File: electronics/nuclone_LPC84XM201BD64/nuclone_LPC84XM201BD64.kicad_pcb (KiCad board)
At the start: 2 copper layers, 48.3 x 76.2 mm, 53 parts, among them J1 JTAG_2X05, J2 USB-ID, J3 nuclone_small_left, J4 nuclone_small_right, SW1 RESET, U1 MCP1702-MB, U2 LPC845M301JBD48, Y1 12MHz

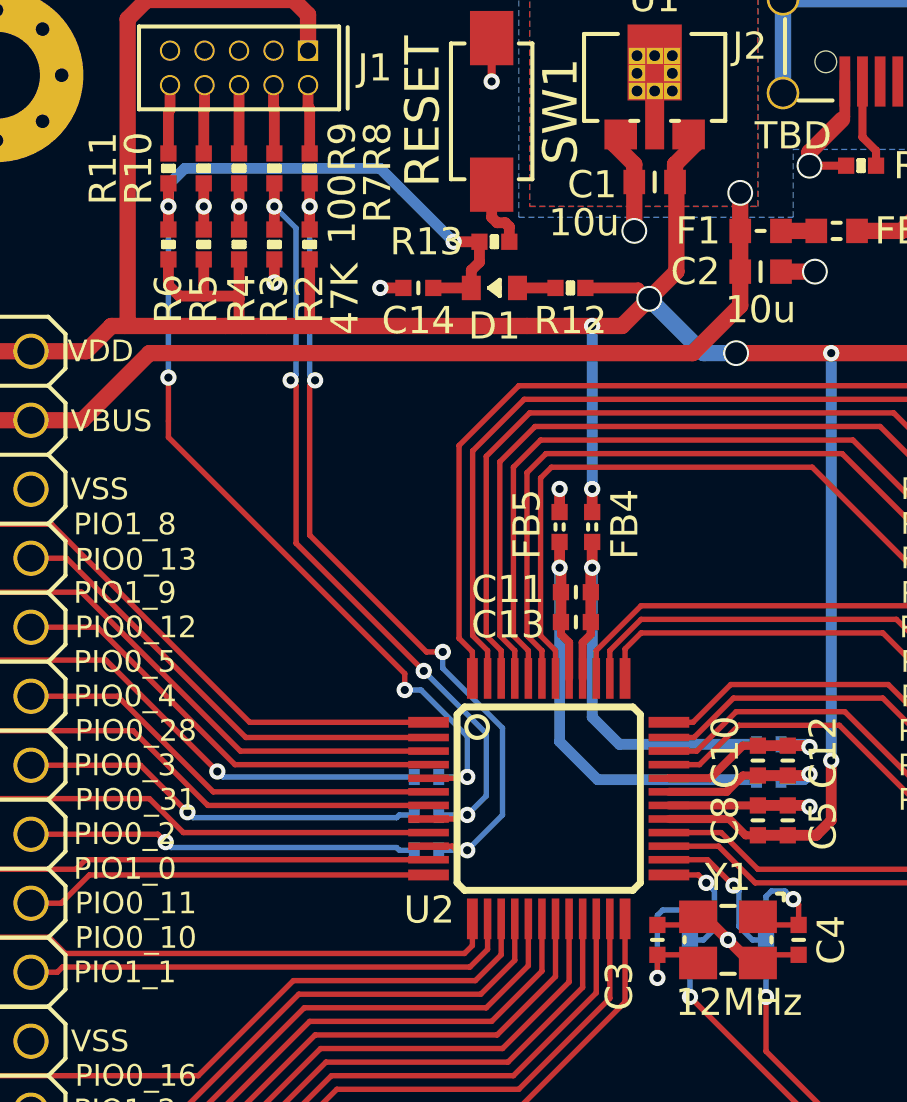
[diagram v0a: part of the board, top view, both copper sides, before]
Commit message: added power led and initial placement, removed old microcontroller
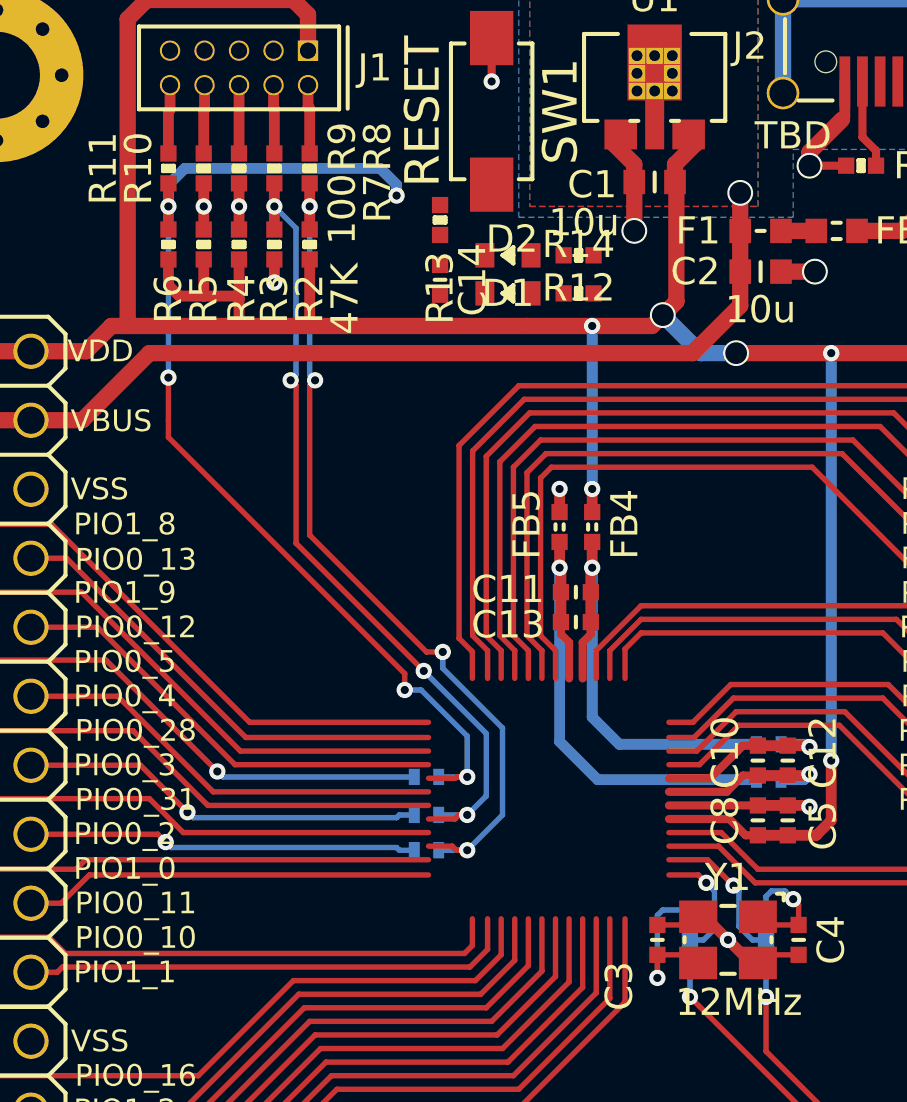
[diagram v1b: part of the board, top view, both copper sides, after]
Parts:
- removed U2: LPC845M301JBD48, SquantorIC:SOT313-2-NXP
- added D2: GREEN, SquantorDiodes:LED_0603_hand, F.Cu at (83.6, 72.8)
- added R14: 10K, SquantorRcl:R_0402_hand, F.Cu at (86.2, 72.8)
- JP1: value PIO0_0 -> PIO0_5
- JP2: value PIO0_10 -> PIO0_3
- JP3: value PIO1_3 -> PIO0_2
- moved R13 2.15 mm to (81.1, 70.1), turned to 90 degrees
- moved D1 1.30 mm to (83.6, 71.4)
- moved R12 1.24 mm to (86.2, 71.4)
- moved C14 0.85 mm to (81.1, 72.3), turned to 90 degrees
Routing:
- net /RESET: track 46.9 -> 40.2 mm
- net /VDD: track 114.7 -> 112.0 mm
- net Net-(R13-Pad2): track 2.55 -> 0.00 mm
- net Net-(D1-Pad2): track 1.40 -> 0.00 mm
- net /VSS: track 26.8 -> 25.9 mm, vias 10 -> 9
